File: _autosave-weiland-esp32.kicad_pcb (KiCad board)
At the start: 2 copper layers, 68.7 x 21.8 mm, 41 parts, among them CN1 SM05B-SRSS-TB (LF)(SN), CN2 SM04B-SRSS-TB (LF)(SN), CN3 SM04B-SRSS-TB (LF)(SN), CN4 SM02B-SRSS-TB (LF)(SN), CN5 SM02B-SRSS-TB (LF)(SN), U1 ESP32-WROOM-32E(8MB), U2 AMS1117-3.3_C347222, U3 MAX98357AETE_T, U5 ULN2003F12FN-7, U6 DZ127S-22-06-55

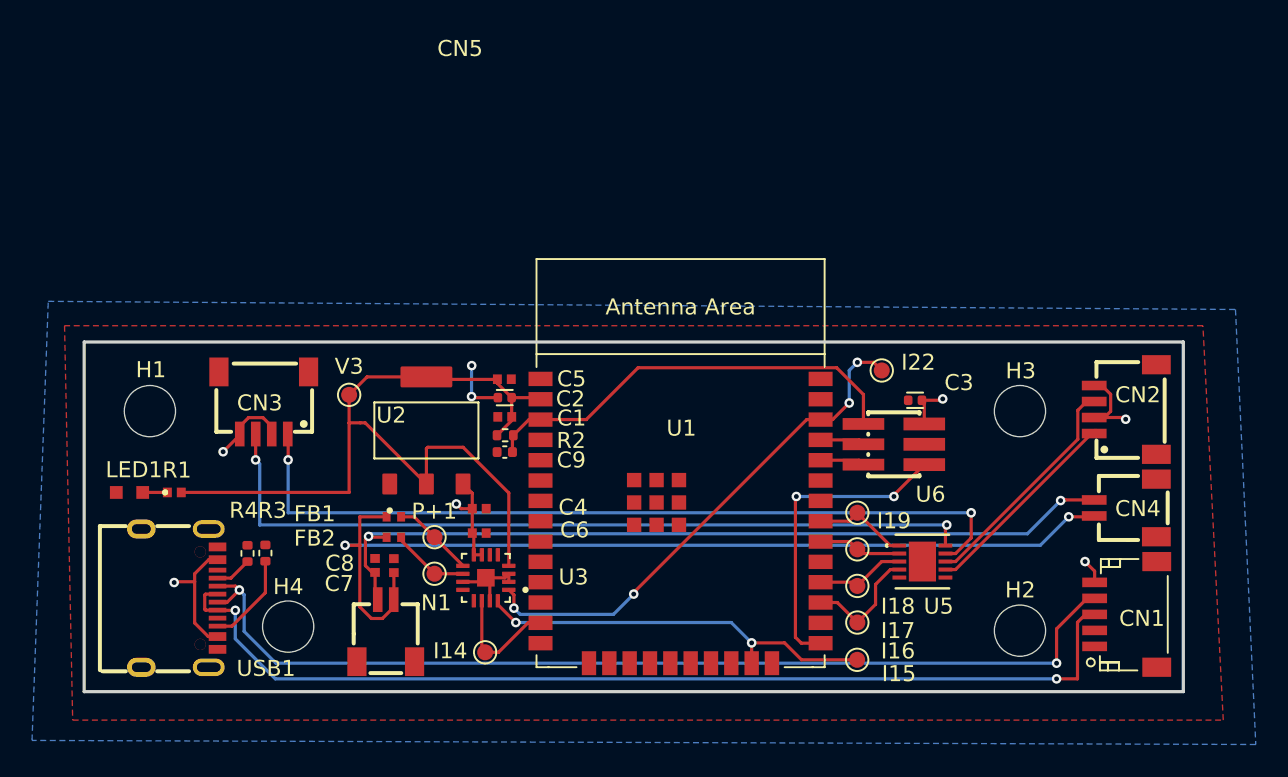
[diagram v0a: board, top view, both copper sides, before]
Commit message: capacitors for ULN2003 and co and coin motors
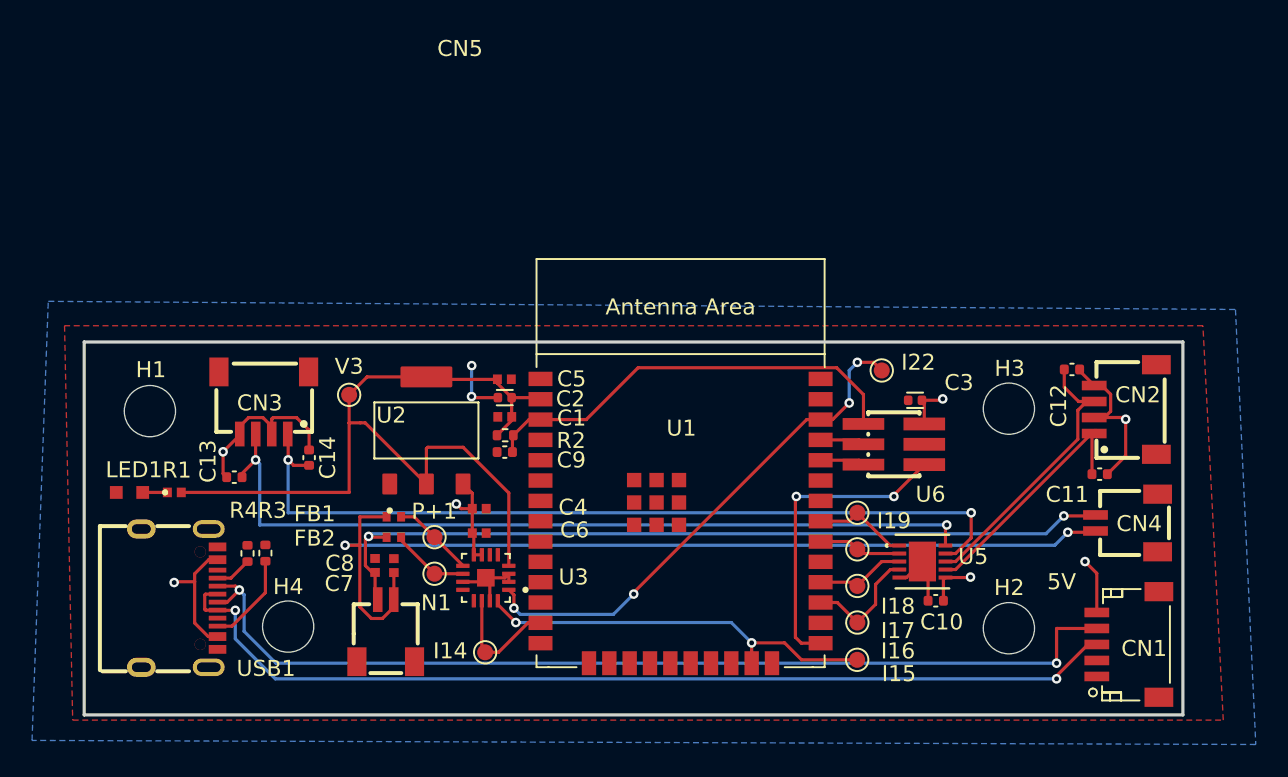
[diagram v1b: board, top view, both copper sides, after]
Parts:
- added C10: 1uF, Capacitor_SMD:C_0402_1005Metric, F.Cu at (186.0, 39.3)
- added C11: 100nF, Capacitor_SMD:C_0402_1005Metric, F.Cu at (196.2, 31.4)
- added C12: 100nF, Capacitor_SMD:C_0402_1005Metric, F.Cu at (194.5, 24.8)
- added C13: 100nF, Capacitor_SMD:C_0402_1005Metric, F.Cu at (142.2, 31.6)
- added C14: 100nF, Capacitor_SMD:C_0402_1005Metric, F.Cu at (146.8, 30.3)
- moved CN1 1.88 mm to (198.0, 42.0)
- moved CN4 0.94 mm to (197.9, 34.4)
- moved H2 0.71 mm to (190.6, 41.0)
- moved H3 0.71 mm to (190.6, 27.3)
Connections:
- U5 pad 6: unconnected-(U5-COM-Pad6) -> +5V
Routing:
- net +5V: track 29.2 -> 46.0 mm, vias 6 -> 7
- net GND: track 9.11 -> 13.6 mm
- net /OUTC: track 14.5 -> 17.8 mm
- net /Dp: track 63.9 -> 61.3 mm
- net /OUTD: track 13.3 -> 15.9 mm
- net /OUTB: track 51.2 -> 52.6 mm
- net /OUTA: track 50.0 -> 51.5 mm
- net /Dn: track 62.7 -> 62.1 mm
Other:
- board size 68.7 x 21.8 mm -> 68.6 x 23.3 mm
- board text added: "5V"
